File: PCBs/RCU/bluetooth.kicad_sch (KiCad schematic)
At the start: 1 part

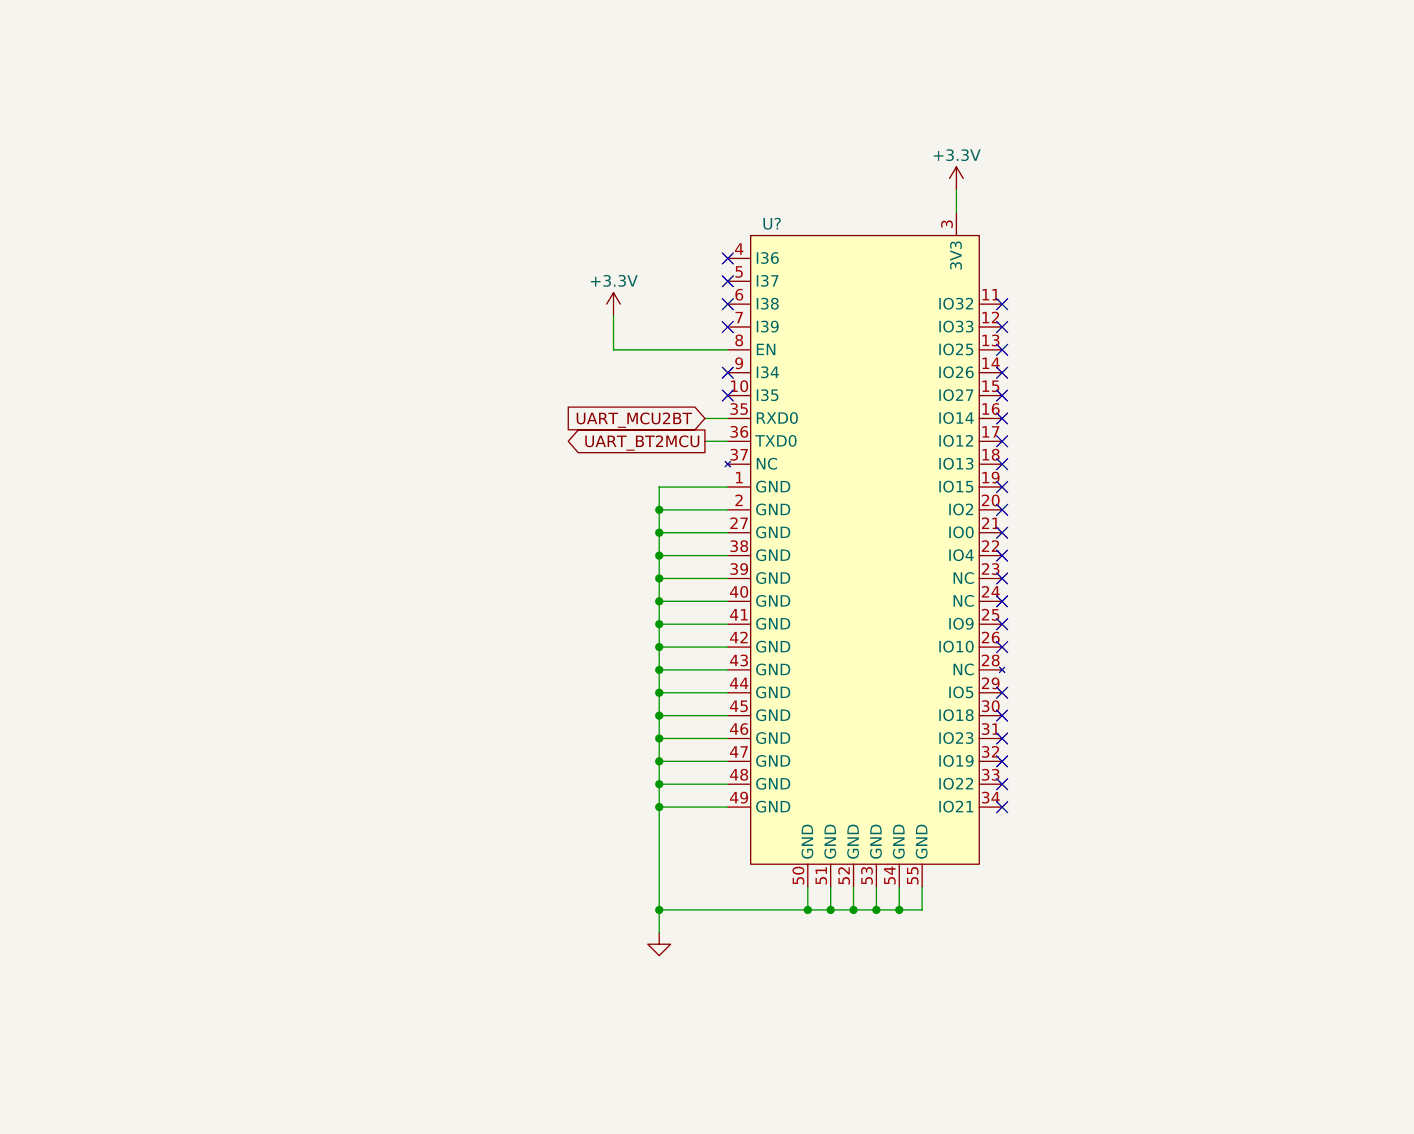
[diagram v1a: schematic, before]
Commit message: Adding programming capability and starting power selector circuit
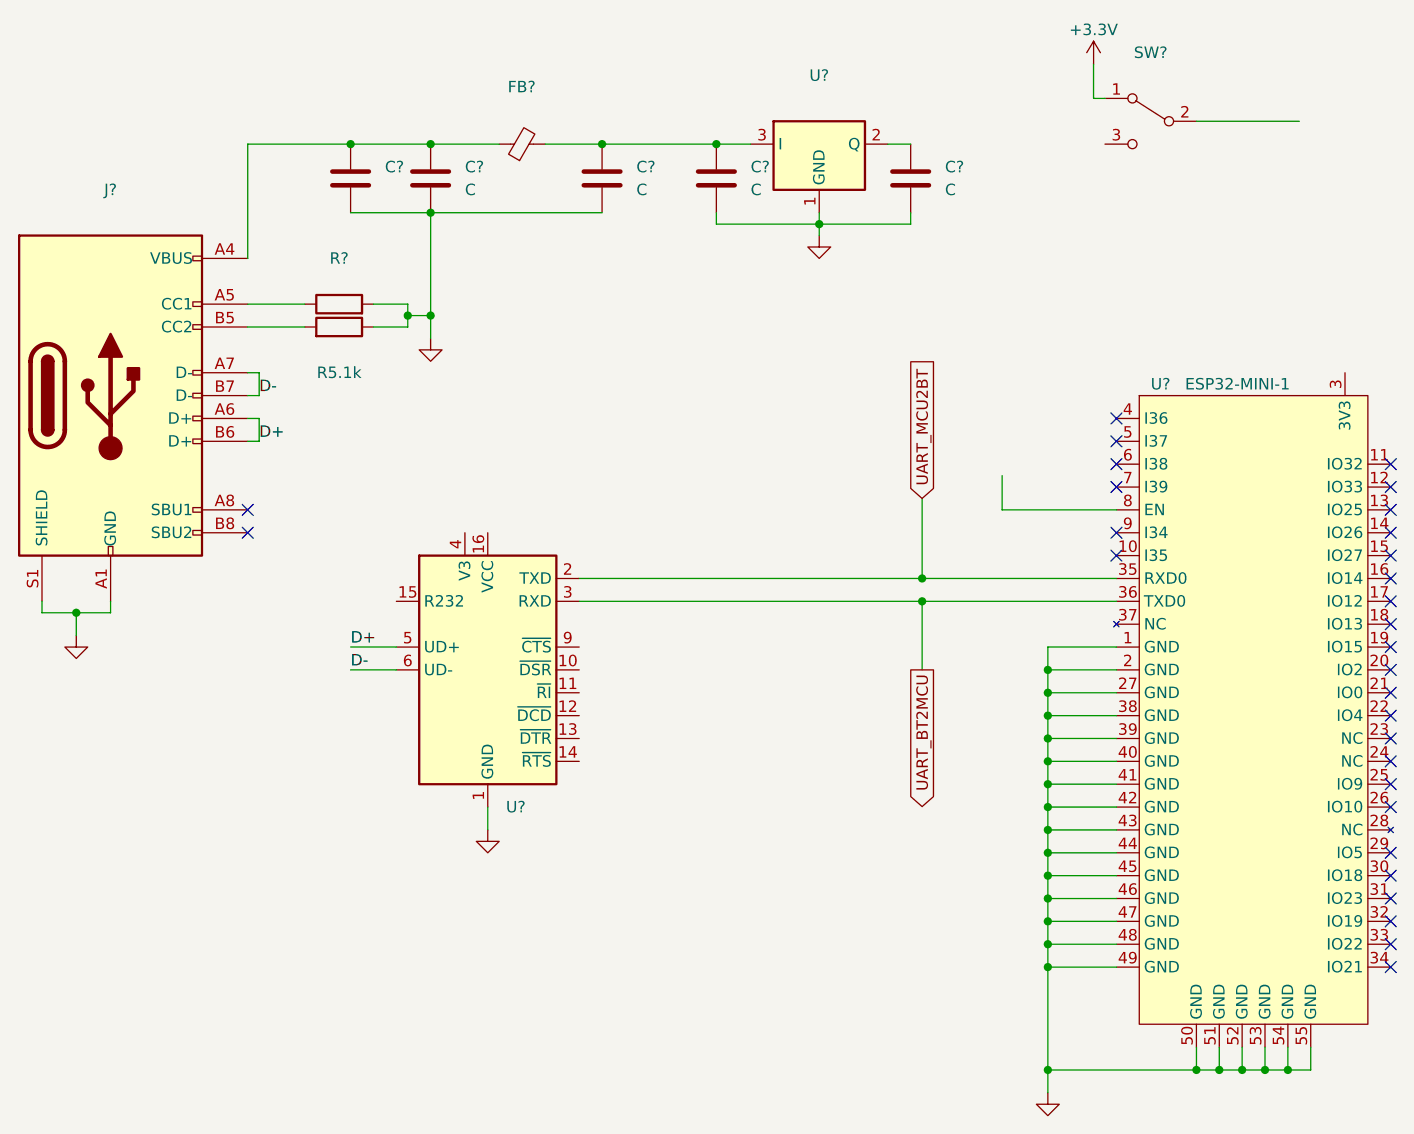
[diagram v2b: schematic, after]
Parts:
- added C? (x4): C, symbol Device:C
- added C?: (no value), symbol Device:C
- added FB?: (no value), symbol Device:FerriteBead_Small
- added J?: (no value), symbol Connector:USB_C_Receptacle_USB2.0
- added R5.1k, R?: (no value), symbol Device:R
- added SW?: (no value), symbol Switch:SW_SPDT
- added U?: (no value), symbol Regulator_Linear:IFX27001TFV15
- added U?: (no value), symbol Interface_USB:CH340C
- U?: value (none) -> ESP32-MINI-1
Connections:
- net +3V3: now also SW?.1 (A); no longer U?.3 (3V3), U?.8 (EN)
- net GND: now also C?.2, C?.2, C?.2, C?.2, C?.2, J?.A1 (GND), J?.A12 (GND), J?.B1 (GND), J?.B12 (GND), J?.S1 (SHIELD), R5.1k.1, R?.2, U?.1 (GND), U?.1 (GND)
- net UART_BT2MCU: now also U?.3 (RXD)
- net UART_MCU2BT: now also U?.2 (TXD)
- new net: C?.1, C?.1, FB?.2, U?.3 (I)
- new net: C?.1, C?.1, FB?.1, J?.A4 (VBUS), J?.A9 (VBUS), J?.B4 (VBUS), J?.B9 (VBUS)
- new net: J?.A5 (CC1), R?.1
- new net: J?.B5 (CC2), R5.1k.2
- new net: C?.1, U?.2 (Q)
- new net D+: J?.A6 (D+), J?.B6 (D+), U?.5 (UD+)
- new net D-: J?.A7 (D-), J?.B7 (D-), U?.6 (UD-)
- no-connect marks 28 -> 30
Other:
- moved on the sheet: U?

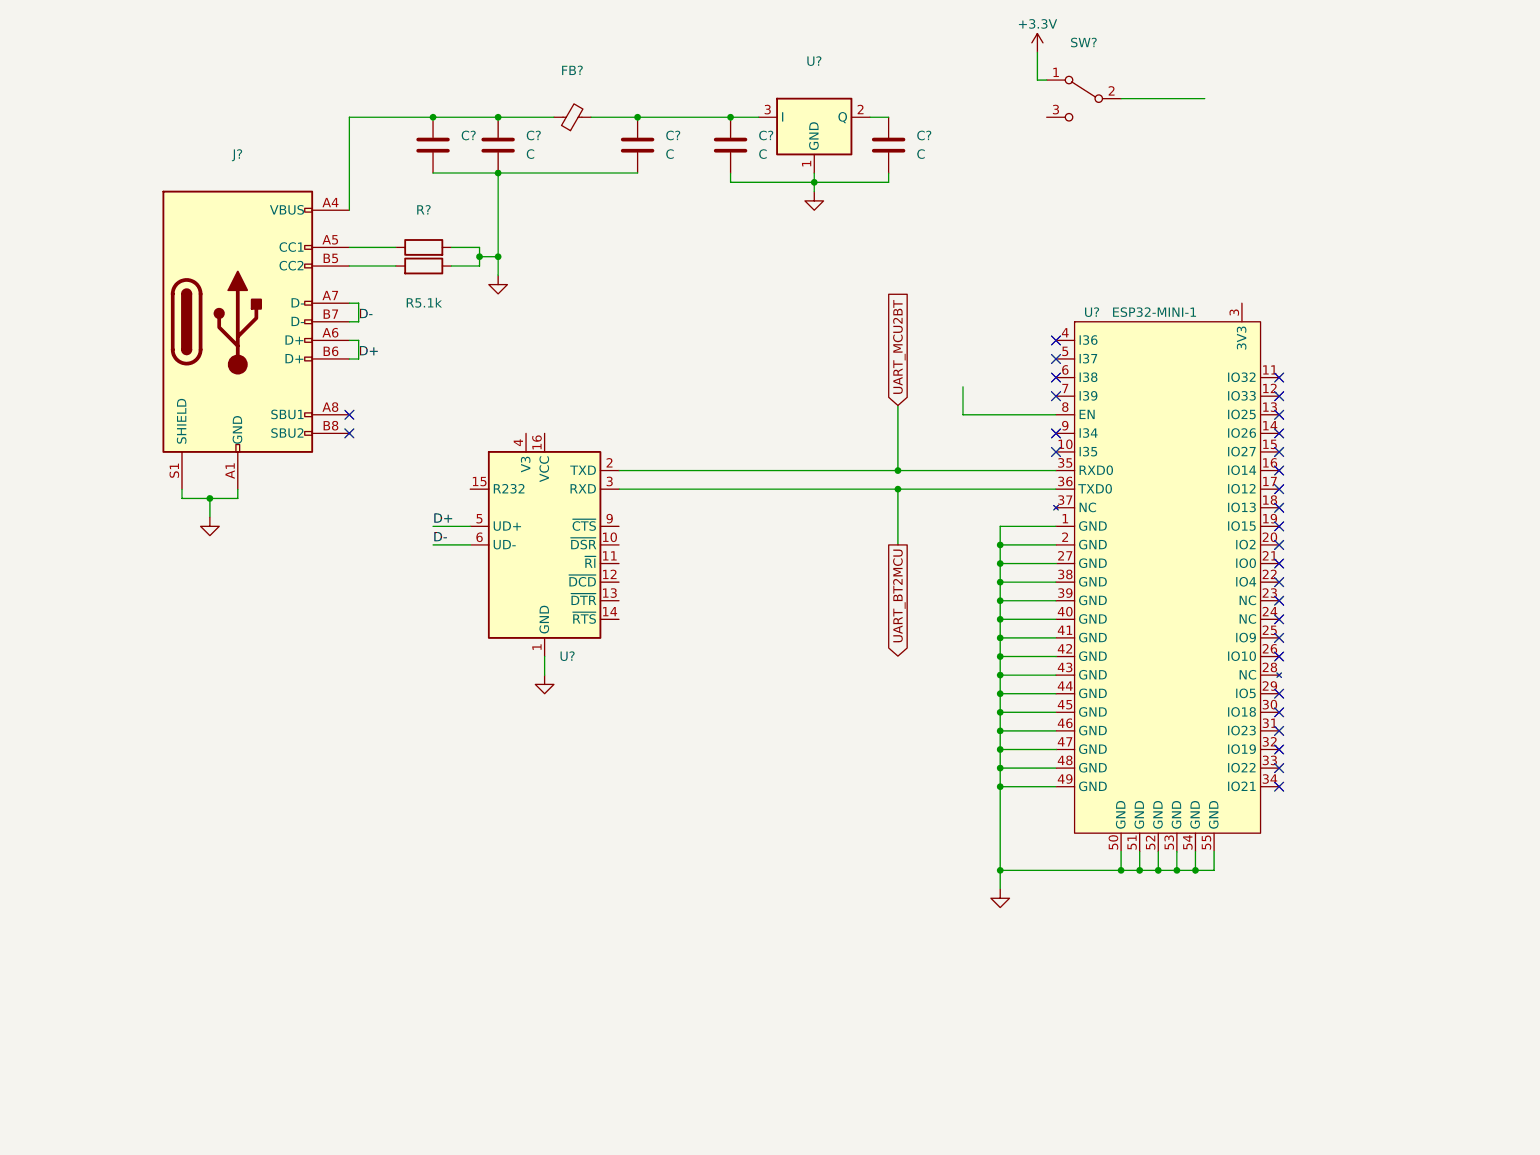
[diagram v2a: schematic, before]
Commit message: Used appropriate names for UART signals
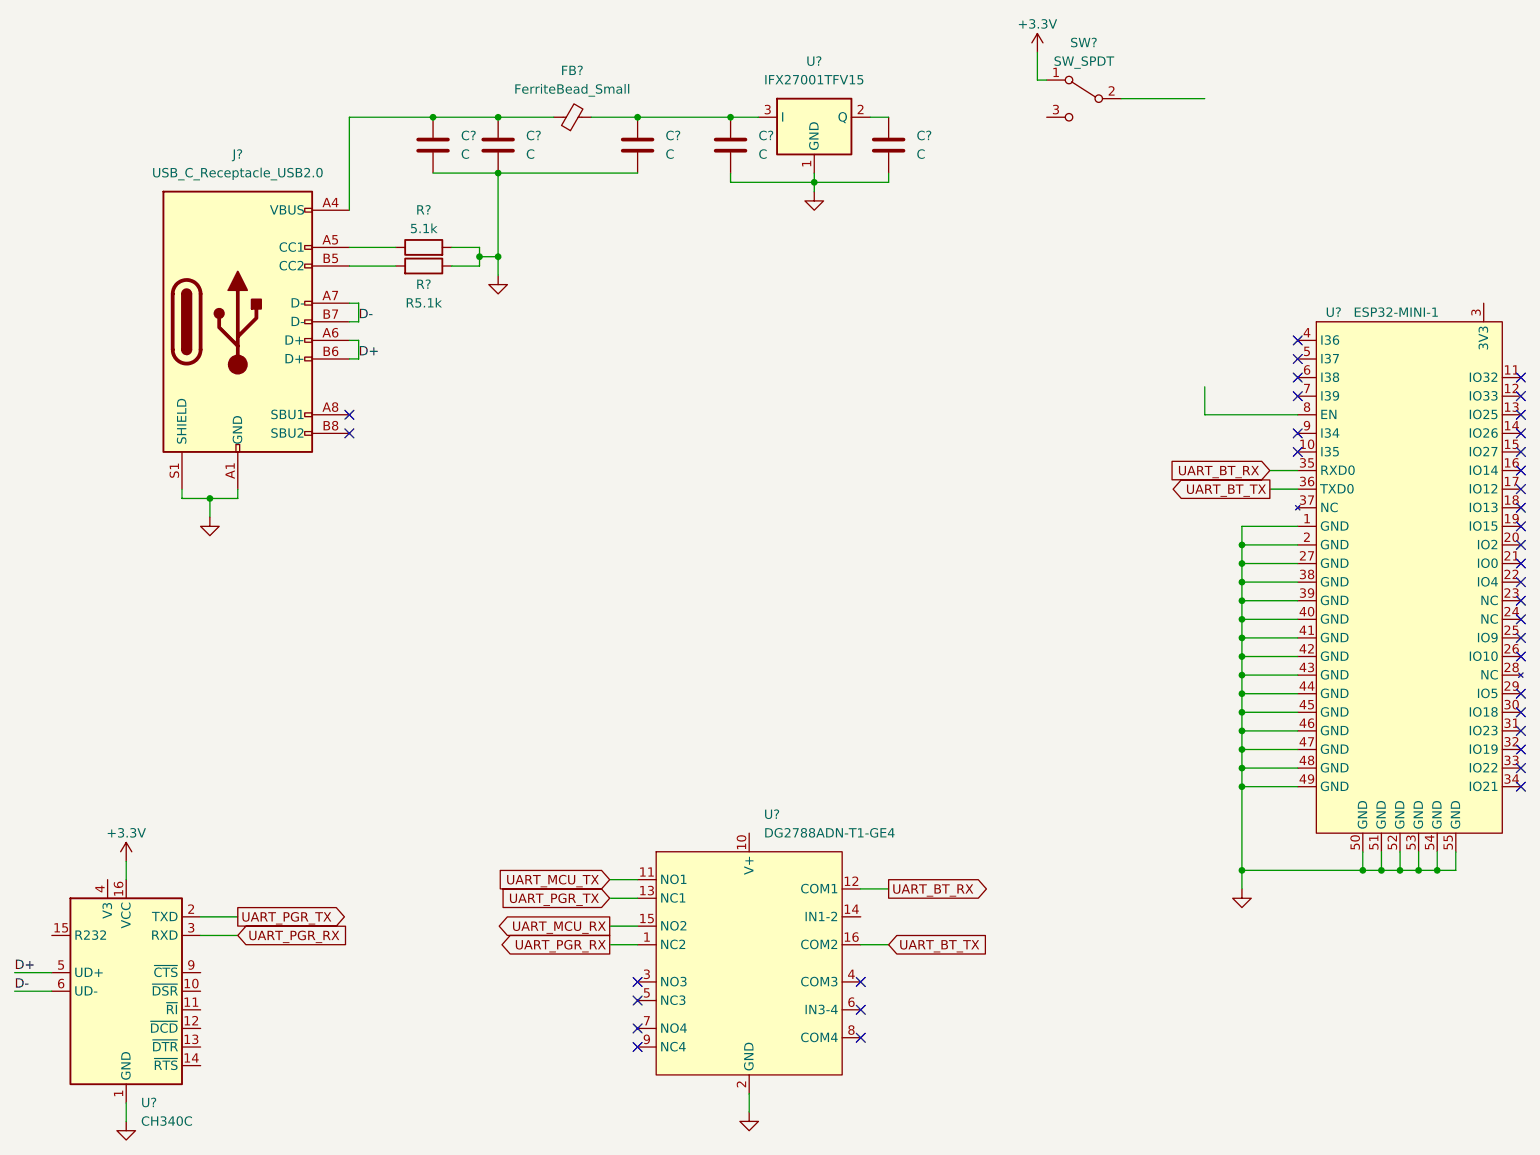
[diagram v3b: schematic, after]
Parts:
- added U?: DG2788ADN-T1-GE4, symbol Ghanis_Symbols_KiCad6:DG2788ADN-T1-GE4
- C?: value (none) -> C
- FB?: value (none) -> FerriteBead_Small
- J?: value (none) -> USB_C_Receptacle_USB2.0
- R5.1k: value (none) -> R?
- R?: value (none) -> 5.1k
- SW?: value (none) -> SW_SPDT
- U?: value (none) -> IFX27001TFV15; footprint (none) -> Package_TO_SOT_SMD:TO-252-3_TabPin2
- U?: value (none) -> CH340C; footprint (none) -> Package_SO:SOIC-16_3.9x9.9mm_P1.27mm
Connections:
- net +3V3: now also U?.16 (VCC)
- net GND: now also U?.2 (GND)
- net UART_BT2MCU renamed UART_BT_TX
- net UART_BT_TX: now also U?.16 (COM2); no longer U?.3 (RXD)
- net UART_MCU2BT renamed UART_BT_RX
- net UART_BT_RX: now also U?.12 (COM1); no longer U?.2 (TXD)
- new net UART_MCU_RX: U?.15 (NO2)
- new net UART_MCU_TX: U?.11 (NO1)
- new net UART_PGR_RX: U?.1 (NC2), U?.3 (RXD)
- new net UART_PGR_TX: U?.13 (NC1), U?.2 (TXD)
- no-connect marks 30 -> 37
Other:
- moved on the sheet: U?
